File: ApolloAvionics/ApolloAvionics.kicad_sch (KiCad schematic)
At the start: 3 parts, among them U1 BMP388, U2 MPU-6000

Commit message: Sensor schematics
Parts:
- added M1: Motor_Servo, symbol Motor:Motor_Servo
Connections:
- net +5V: now also U2.1 (VCC), M1.2 (+)
- net GND: now also U2.2 (GND), M1.3 (-)
- net at A1.19 (A0): now also M1.1 (PWM)
- net at A1.23 (A4): now also U1.6 (SDA), U2.4 (SDA)
- net at A1.24 (A5): now also U1.4 (SCL), U2.3 (SCL)
- no-connect marks 26 -> 30
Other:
- moved on the sheet: A1, U1

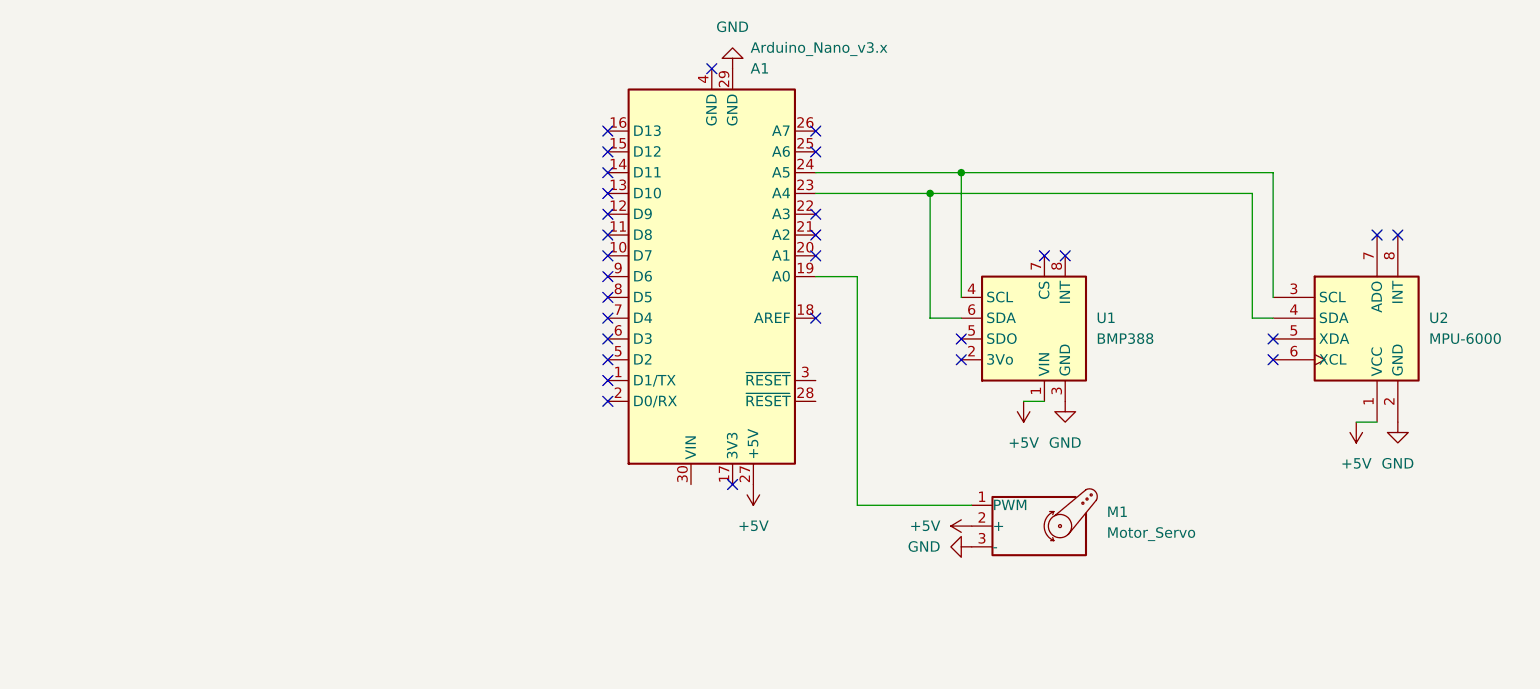
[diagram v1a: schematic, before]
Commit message: Added Motor and Battery Schematics
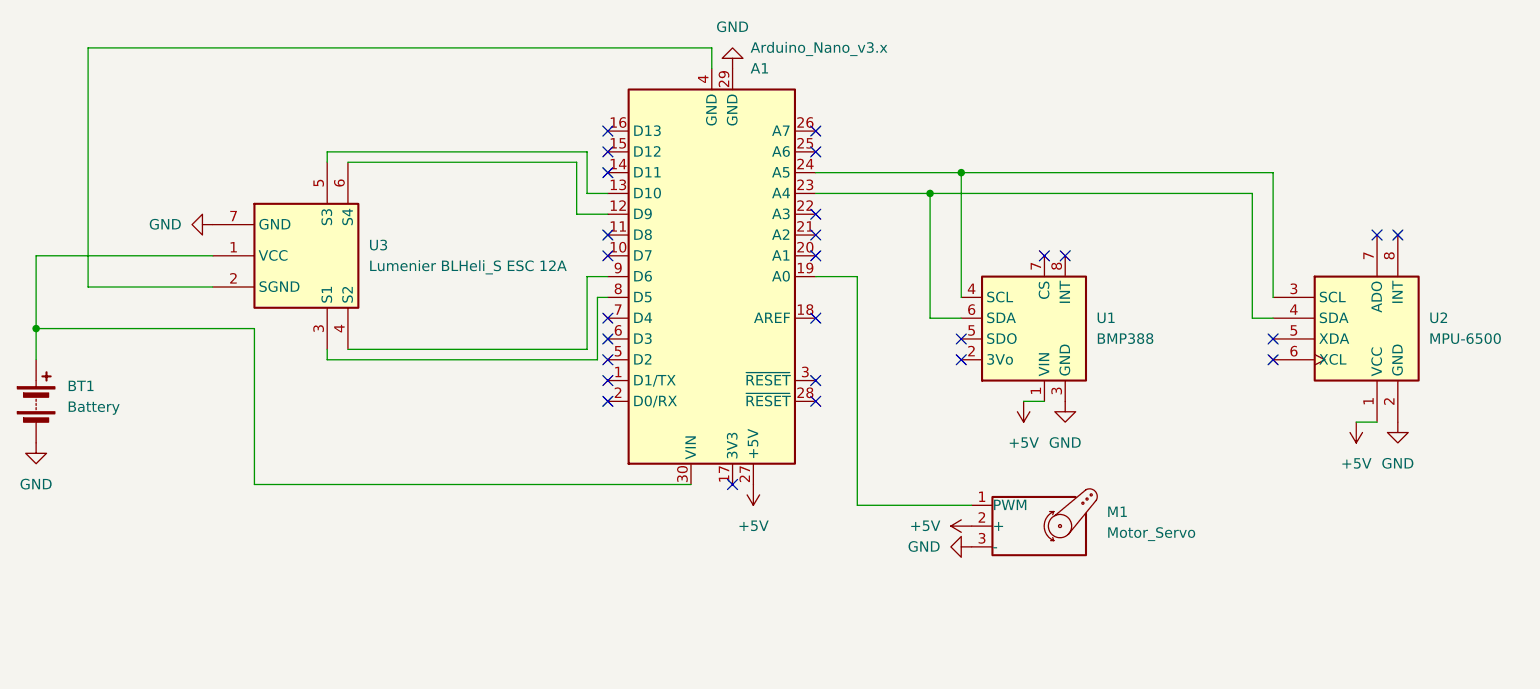
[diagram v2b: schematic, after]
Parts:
- added BT1: Battery, Connector_BarrelJack:BarrelJack_SwitchcraftConxall_RAPC10U_Horizontal, symbol Device:Battery
- added U3: Lumenier BLHeli_S ESC 12A, Connector_PinSocket_2.54mm:PinSocket_1x07_P2.54mm_Vertical, symbol Sensor_Motion:MPU-6000
- M1: footprint (none) -> Connector_PinSocket_2.54mm:PinSocket_1x03_P2.54mm_Vertical
- U2: value MPU-6000 -> MPU-6500
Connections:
- net GND: now also BT1.2 (-), U3.7 (GND)
- net at A1.12 (D9): now also U3.6 (S4)
- net at A1.13 (D10): now also U3.5 (S3)
- net at A1.30 (VIN): now also BT1.1 (+), U3.1 (VCC)
- net at A1.4 (GND): now also U3.2 (SGND)
- net at A1.8 (D5): now also U3.3 (S1)
- net at A1.9 (D6): now also U3.4 (S2)
- no-connect marks 30 -> 27
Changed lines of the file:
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@@
   (junction (at 129.54 80.01) (diameter 0) (color 0 0 0 0)
+  )
+  (junction (at 20.32 96.52) (diameter 0) (color 0 0 0 0)
   )
   (no_connect (at 90.17 97.79))
@@
   (no_connect (at 90.17 100.33))
   (no_connect (at 115.57 74.93))
+  (no_connect (at 115.57 102.87))
   (no_connect (at 90.17 85.09))
-  (no_connect (at 90.17 80.01))
   (no_connect (at 171.45 97.79))
   (no_connect (at 105.41 115.57))
   (no_connect (at 186.69 85.09))
-  (no_connect (at 90.17 82.55))
   (no_connect (at 115.57 95.25))
   (no_connect (at 146.05 87.63))
   (no_connect (at 90.17 87.63))
   (no_connect (at 115.57 82.55))
-  (no_connect (at 102.87 64.77))
   (no_connect (at 90.17 105.41))
   (no_connect (at 90.17 95.25))
   (no_connect (at 143.51 87.63))
+  (no_connect (at 115.57 105.41))
   (no_connect (at 90.17 77.47))
   (no_connect (at 115.57 85.09))
-  (no_connect (at 90.17 92.71))
   (no_connect (at 90.17 72.39))
   (no_connect (at 133.35 100.33))
   (no_connect (at 184.15 85.09))
-  (no_connect (at 90.17 90.17))
   (no_connect (at 171.45 100.33))
   (no_connect (at 90.17 74.93))
   (no_connect (at 115.57 72.39))
+  (wire (pts (xy 102.87 62.23) (xy 102.87 64.77))
+    (stroke (width 0) (type default))
+  )
   (wire (pts (xy 120.65 118.11) (xy 120.65 90.17))
     (stroke (width 0) (type default))
@@
     (stroke (width 0) (type default))
   )
+  (wire (pts (xy 20.32 87.63) (xy 41.91 87.63))
+    (stroke (width 0) (type default))
+  )
+  (wire (pts (xy 87.63 90.17) (xy 90.17 90.17))
+    (stroke (width 0) (type default))
+  )
+  (wire (pts (xy 86.36 76.2) (xy 86.36 82.55))
+    (stroke (width 0) (type default))
+  )
   (wire (pts (xy 129.54 95.25) (xy 129.54 80.01))
     (stroke (width 0) (type default))
   )
+  (wire (pts (xy 88.9 92.71) (xy 90.17 92.71))
+    (stroke (width 0) (type default))
+  )
+  (wire (pts (xy 86.36 82.55) (xy 90.17 82.55))
+    (stroke (width 0) (type default))
+  )
+  (wire (pts (xy 26.67 62.23) (xy 102.87 62.23))
+    (stroke (width 0) (type default))
+  )
+  (wire (pts (xy 87.63 74.93) (xy 87.63 80.01))
+    (stroke (width 0) (type default))
+  )
+  (wire (pts (xy 88.9 100.33) (xy 88.9 92.71))
+    (stroke (width 0) (type default))
+  )
   (wire (pts (xy 129.54 80.01) (xy 168.91 80.01))
     (stroke (width 0) (type default))
   )
+  (wire (pts (xy 58.42 76.2) (xy 86.36 76.2))
+    (stroke (width 0) (type default))
+  )
+  (wire (pts (xy 58.42 99.06) (xy 87.63 99.06))
+    (stroke (width 0) (type default))
+  )
   (wire (pts (xy 171.45 92.71) (xy 171.45 77.47))
     (stroke (width 0) (type default))
@@
     (stroke (width 0) (type default))
   )
+  (wire (pts (xy 55.88 100.33) (xy 88.9 100.33))
+    (stroke (width 0) (type default))
+  )
+  (wire (pts (xy 20.32 96.52) (xy 20.32 87.63))
+    (stroke (width 0) (type default))
+  )
+  (wire (pts (xy 46.99 96.52) (xy 46.99 115.57))
+    (stroke (width 0) (type default))
+  )
   (wire (pts (xy 171.45 77.47) (xy 133.35 77.47))
     (stroke (width 0) (type default))
   )
+  (wire (pts (xy 55.88 76.2) (xy 55.88 74.93))
+    (stroke (width 0) (type default))
+  )
+  (wire (pts (xy 87.63 80.01) (xy 90.17 80.01))
+    (stroke (width 0) (type default))
+  )
+  (wire (pts (xy 55.88 74.93) (xy 87.63 74.93))
+    (stroke (width 0) (type default))
+  )
   (wire (pts (xy 168.91 80.01) (xy 168.91 95.25))
     (stroke (width 0) (type default))
@@
     (stroke (width 0) (type default))
   )
+  (wire (pts (xy 20.32 100.33) (xy 20.32 96.52))
+    (stroke (width 0) (type default))
+  )
+  (wire (pts (xy 55.88 99.06) (xy 55.88 100.33))
+    (stroke (width 0) (type default))
+  )
+  (wire (pts (xy 87.63 90.17) (xy 87.63 99.06))
+    (stroke (width 0) (type default))
+  )
+  (wire (pts (xy 46.99 115.57) (xy 100.33 115.57))
+    (stroke (width 0) (type default))
+  )
+  (wire (pts (xy 20.32 96.52) (xy 46.99 96.52))
+    (stroke (width 0) (type default))
+  )
   (wire (pts (xy 168.91 95.25) (xy 171.45 95.25))
     (stroke (width 0) (type default))
@@
     (stroke (width 0) (type default))
   )
+  (wire (pts (xy 41.91 91.44) (xy 26.67 91.44))
+    (stroke (width 0) (type default))
+  )
   (wire (pts (xy 115.57 80.01) (xy 129.54 80.01))
     (stroke (width 0) (type default))
@@
   (wire (pts (xy 140.97 105.41) (xy 143.51 105.41))
     (stroke (width 0) (type default))
+  )
+  (wire (pts (xy 26.67 91.44) (xy 26.67 62.23))
+    (stroke (width 0) (type default))
+  )
+  (symbol (lib_name "MPU-6000_1") (lib_id "Sensor_Motion:MPU-6000") (at 53.34 87.63 0) (unit 1)
+    (in_bom yes) (on_board yes) (dnp no) (fields_autoplaced)
+    (property "Reference" "U3" (at 60.96 86.36 0)
+      (effects (font (size 1.27 1.27)) (justify left))
+    )
+    (property "Value" "Lumenier BLHeli_S ESC 12A" (at 60.96 88.9 0)
+      (effects (font (size 1.27 1.27)) (justify left))
+    )
+    (property "Footprint" "Connector_PinSocket_2.54mm:PinSocket_1x07_P2.54mm_Vertical" (at 53.34 107.95 0)
+      (effects (font (size 1.27 1.27)) hide)
+    )
+    (property "Datasheet" "" (at 52.07 83.82 90)
+      (effects (font (size 1.27 1.27)) hide)
+    )
+    (pin "1")
+    (pin "3")
+    (pin "6")
+    (pin "7")
+    (pin "4")
+    (pin "2")
+    (pin "5")
+    (instances
+      (project "ApolloAvionics"
+        (path "/7bce98ec-64a0-43c6-a27f-97096f895589"
+          (reference "U3") (unit 1)
+        )
+      )
+    )
   )
   (symbol (lib_id "power:+5V") (at 140.97 105.41 0) (mirror x) (unit 1)
@@
     )
   )
+  (symbol (lib_id "Device:Battery") (at 20.32 105.41 0) (unit 1)
+    (in_bom yes) (on_board yes) (dnp no) (fields_autoplaced)
+    (property "Reference" "BT1" (at 24.13 103.5685 0)
+      (effects (font (size 1.27 1.27)) (justify left))
+    )
+    (property "Value" "Battery" (at 24.13 106.1085 0)
+      (effects (font (size 1.27 1.27)) (justify left))
+    )
+    (property "Footprint" "Connector_BarrelJack:BarrelJack_SwitchcraftConxall_RAPC10U_Horizontal" (at 20.32 103.886 90)
+      (effects (font (size 1.27 1.27)) hide)
+    )
+    (property "Datasheet" "~" (at 20.32 103.886 90)
+      (effects (font (size 1.27 1.27)) hide)
+    )
+    (pin "2")
+    (pin "1")
+    (instances
+      (project "ApolloAvionics"
+        (path "/7bce98ec-64a0-43c6-a27f-97096f895589"
+          (reference "BT1") (unit 1)
+        )
+      )
+    )
+  )
   (symbol (lib_id "power:+5V") (at 107.95 115.57 0) (mirror x) (unit 1)
     (in_bom yes) (on_board yes) (dnp no) (fields_autoplaced)
@@
         (path "/7bce98ec-64a0-43c6-a27f-97096f895589"
           (reference "#PWR05") (unit 1)
+        )
+      )
+    )
+  )
+  (symbol (lib_id "power:GND") (at 20.32 110.49 0) (unit 1)
+    (in_bom yes) (on_board yes) (dnp no) (fields_autoplaced)
+    (property "Reference" "#PWR010" (at 20.32 116.84 0)
+      (effects (font (size 1.27 1.27)) hide)
+    )
+    (property "Value" "GND" (at 20.32 115.57 0)
+      (effects (font (size 1.27 1.27)))
+    )
+    (property "Footprint" "" (at 20.32 110.49 0)
+      (effects (font (size 1.27 1.27)) hide)
+    )
+    (property "Datasheet" "" (at 20.32 110.49 0)
+      (effects (font (size 1.27 1.27)) hide)
+    )
+    (pin "1")
+    (instances
+      (project "ApolloAvionics"
+        (path "/7bce98ec-64a0-43c6-a27f-97096f895589"
+          (reference "#PWR010") (unit 1)
         )
       )
@@
     )
   )
+  (symbol (lib_id "power:GND") (at 41.91 83.82 270) (unit 1)
+    (in_bom yes) (on_board yes) (dnp no) (fields_autoplaced)
+    (property "Reference" "#PWR09" (at 35.56 83.82 0)
+      (effects (font (size 1.27 1.27)) hide)
+    )
+    (property "Value" "GND" (at 38.1 83.82 90)
+      (effects (font (size 1.27 1.27)) (justify right))
+    )
+    (property "Footprint" "" (at 41.91 83.82 0)
+      (effects (font (size 1.27 1.27)) hide)
+    )
+    (property "Datasheet" "" (at 41.91 83.82 0)
+      (effects (font (size 1.27 1.27)) hide)
+    )
+    (pin "1")
+    (instances
+      (project "ApolloAvionics"
+        (path "/7bce98ec-64a0-43c6-a27f-97096f895589"
+          (reference "#PWR09") (unit 1)
+        )
+      )
+    )
+  )
   (symbol (lib_id "Sensor_Motion:MPU-6000") (at 182.88 96.52 0) (unit 1)
     (in_bom yes) (on_board yes) (dnp no) (fields_autoplaced)
@@
       (effects (font (size 1.27 1.27)) (justify left))
     )
-    (property "Value" "MPU-6000" (at 190.5 97.79 0)
+    (property "Value" "MPU-6500" (at 190.5 97.79 0)
       (effects (font (size 1.27 1.27)) (justify left))
     )
@@
       (effects (font (size 1.27 1.27)) (justify left))
     )
-    (property "Footprint" "" (at 142.24 125.476 0)
-      (effects (font (size 1.27 1.27)) hide)
-    )
+    (property "Footprint" "Connector_PinSocket_2.54mm:PinSocket_1x03_P2.54mm_Vertical" (at 142.24 125.476 0)
+      (effects (font (size 1.27 1.27)) hide)
+    )

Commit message: Finalized PCB and setup velocity function
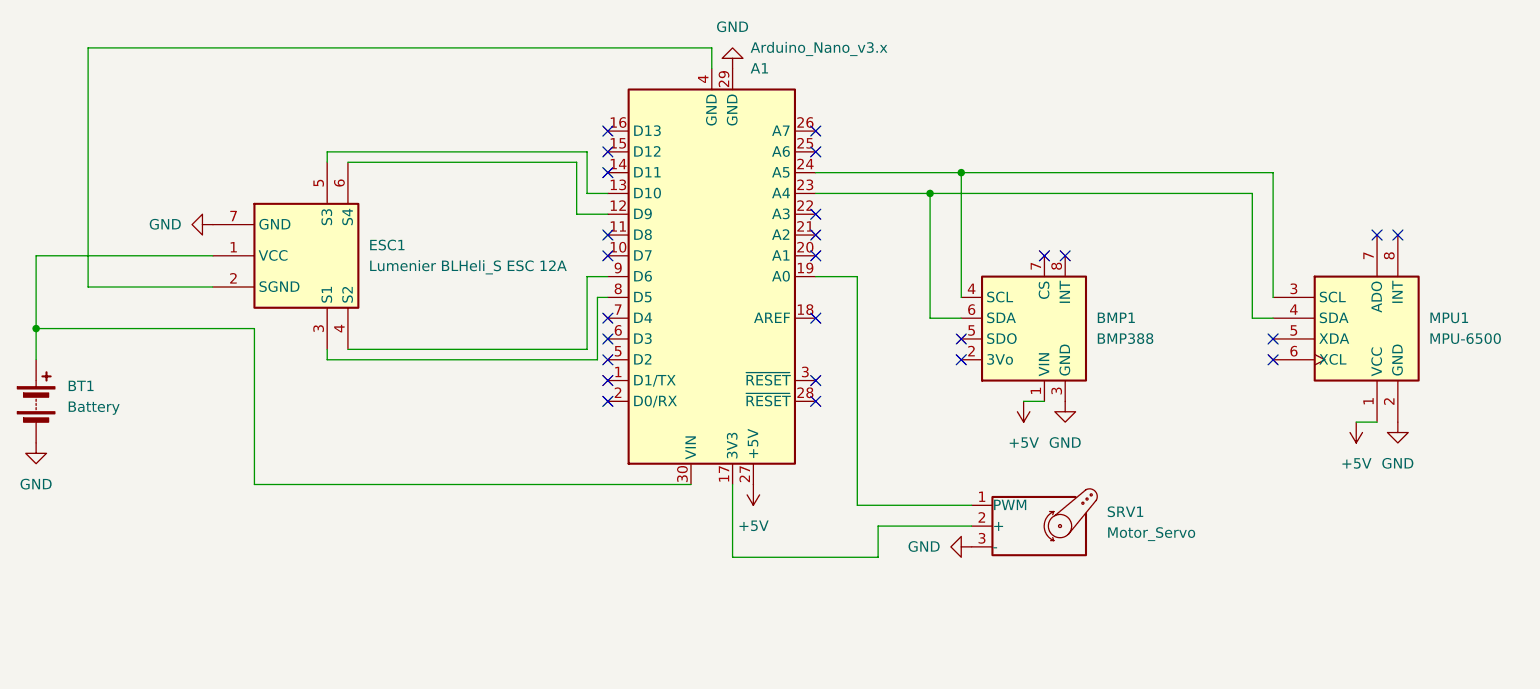
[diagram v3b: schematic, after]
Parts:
- BT1: footprint Connector_BarrelJack:BarrelJack_SwitchcraftConxall_RAPC10U_Horizontal -> Connector_PinSocket_2.54mm:PinSocket_1x02_P2.54mm_Vertical
- renumbered U1 to BMP1, U3 to ESC1, U2 to MPU1, M1 to SRV1
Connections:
- net +5V: no longer SRV1.2 (+)
- net at A1.17 (3V3): now also SRV1.2 (+)
- no-connect marks 27 -> 26
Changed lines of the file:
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@@
   (no_connect (at 90.17 85.09))
   (no_connect (at 171.45 97.79))
-  (no_connect (at 105.41 115.57))
   (no_connect (at 186.69 85.09))
   (no_connect (at 115.57 95.25))
@@
     (stroke (width 0) (type default))
   )
+  (wire (pts (xy 123.19 124.46) (xy 123.19 120.65))
+    (stroke (width 0) (type default))
+  )
   (wire (pts (xy 87.63 90.17) (xy 90.17 90.17))
     (stroke (width 0) (type default))
@@
     (stroke (width 0) (type default))
   )
+  (wire (pts (xy 123.19 120.65) (xy 134.62 120.65))
+    (stroke (width 0) (type default))
+  )
   (wire (pts (xy 20.32 100.33) (xy 20.32 96.52))
     (stroke (width 0) (type default))
@@
     (stroke (width 0) (type default))
   )
+  (wire (pts (xy 105.41 124.46) (xy 123.19 124.46))
+    (stroke (width 0) (type default))
+  )
   (wire (pts (xy 41.91 91.44) (xy 26.67 91.44))
     (stroke (width 0) (type default))
   )
+  (wire (pts (xy 105.41 115.57) (xy 105.41 124.46))
+    (stroke (width 0) (type default))
+  )
   (wire (pts (xy 115.57 80.01) (xy 129.54 80.01))
     (stroke (width 0) (type default))
@@
   (symbol (lib_name "MPU-6000_1") (lib_id "Sensor_Motion:MPU-6000") (at 53.34 87.63 0) (unit 1)
     (in_bom yes) (on_board yes) (dnp no) (fields_autoplaced)
-    (property "Reference" "U3" (at 60.96 86.36 0)
+    (property "Reference" "ESC1" (at 60.96 86.36 0)
       (effects (font (size 1.27 1.27)) (justify left))
     )
@@
       (project "ApolloAvionics"
         (path "/7bce98ec-64a0-43c6-a27f-97096f895589"
-          (reference "U3") (unit 1)
+          (reference "ESC1") (unit 1)
         )
       )
@@
       (effects (font (size 1.27 1.27)) (justify left))
     )
-    (property "Footprint" "Connector_BarrelJack:BarrelJack_SwitchcraftConxall_RAPC10U_Horizontal" (at 20.32 103.886 90)
+    (property "Footprint" "Connector_PinSocket_2.54mm:PinSocket_1x02_P2.54mm_Vertical" (at 20.32 103.886 90)
       (effects (font (size 1.27 1.27)) hide)
     )
@@
   (symbol (lib_id "Sensor_Motion:MPU-6000") (at 182.88 96.52 0) (unit 1)
     (in_bom yes) (on_board yes) (dnp no) (fields_autoplaced)
-    (property "Reference" "U2" (at 190.5 95.25 0)
+    (property "Reference" "MPU1" (at 190.5 95.25 0)
       (effects (font (size 1.27 1.27)) (justify left))
     )
@@
       (project "ApolloAvionics"
         (path "/7bce98ec-64a0-43c6-a27f-97096f895589"
-          (reference "U2") (unit 1)
+          (reference "MPU1") (unit 1)
         )
       )
@@
   (symbol (lib_id "Motor:Motor_Servo") (at 142.24 120.65 0) (unit 1)
     (in_bom yes) (on_board yes) (dnp no) (fields_autoplaced)
-    (property "Reference" "M1" (at 151.13 118.9466 0)
+    (property "Reference" "SRV1" (at 151.13 118.9466 0)
       (effects (font (size 1.27 1.27)) (justify left))
     )
@@
       (project "ApolloAvionics"
         (path "/7bce98ec-64a0-43c6-a27f-97096f895589"
-          (reference "M1") (unit 1)
-        )
-      )
-    )
-  )
-  (symbol (lib_id "power:+5V") (at 134.62 120.65 90) (mirror x) (unit 1)
-    (in_bom yes) (on_board yes) (dnp no)
-    (property "Reference" "#PWR07" (at 138.43 120.65 0)
-      (effects (font (size 1.27 1.27)) hide)
-    )
-    (property "Value" "+5V" (at 130.81 120.65 90)
-      (effects (font (size 1.27 1.27)) (justify left))
-    )
-    (property "Footprint" "" (at 134.62 120.65 0)
-      (effects (font (size 1.27 1.27)) hide)
-    )
-    (property "Datasheet" "" (at 134.62 120.65 0)
-      (effects (font (size 1.27 1.27)) hide)
-    )
-    (pin "1")
-    (instances
-      (project "ApolloAvionics"
-        (path "/7bce98ec-64a0-43c6-a27f-97096f895589"
-          (reference "#PWR07") (unit 1)
+          (reference "SRV1") (unit 1)
         )
       )
@@
   (symbol (lib_id "Sensor_Pressure:BMP280") (at 143.51 97.79 0) (unit 1)
     (in_bom yes) (on_board yes) (dnp no) (fields_autoplaced)
-    (property "Reference" "U1" (at 149.86 95.25 0)
+    (property "Reference" "BMP1" (at 149.86 95.25 0)
       (effects (font (size 1.27 1.27)) (justify left))
     )
@@
       (project "ApolloAvionics"
         (path "/7bce98ec-64a0-43c6-a27f-97096f895589"
-          (reference "U1") (unit 1)
-        )
-      )
+          (reference "BMP1") (unit 1)
+        )
+      )
